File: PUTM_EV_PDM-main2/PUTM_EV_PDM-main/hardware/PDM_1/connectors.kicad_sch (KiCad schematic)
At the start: 3 parts, among them J3 UPT-08-03.0-01-L-V, J4 UPT-08-03.0-01-L-V, J5 UPT-02-01-01-X-RA

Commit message: piny na płytce
Dodano ułożenie pinów na płytce
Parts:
- removed J3, J4: UPT-08-03.0-01-L-V, UPT-08-03.0-01-L-V:SAMTEC_UPT-08-03.0-01-L-V, symbol 8pin:UPT-08-03.0-01-L-V
- added J2, J7: UPT-08-01-01-L-RA, UPT080101LRA, symbol 8pin_good:UPT-08-01-01-L-RA
- added J6: Conn_01x06, Connector_IDC:IDC-Header_2x03_P2.54mm_Vertical, symbol Connector_Generic:Conn_01x06
- J5: footprint UPT-02-01-01-X-RA:SAMTEC_UPT-02-01-01-X-RA -> 2pin:SAMTEC_UPT-02-01-01-X-RA
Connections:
- net +BATT: now reaches J5.P01_1 (01)
- net GND: now reaches J5.P02_1 (02)
- net GND: now also J6.4 (Pin_4), J6.5 (Pin_5), J6.6 (Pin_6), J7.A1, J7.A2, J7.A3, J7.A4, J7.A5, J7.A6
- new net ASMS: J6.3 (Pin_3)
- new net CAN_H: J6.2 (Pin_2)
- new net CAN_L: J6.1 (Pin_1)
- new net OUT1_0: J2.A1, J2.A2, J2.A3, J2.A4, J2.A5, J2.A6
- new net OUT1_1: J2.B1, J2.B2, J2.B3, J2.B4, J2.B5, J2.B6
- new net OUT1_2: J2.C1, J2.C2, J2.C3, J2.C4, J2.C5, J2.C6
- new net OUT1_3: J2.D1, J2.D2, J2.D3, J2.D4, J2.D5, J2.D6
- new net OUT2_0: J2.E1, J2.E2, J2.E3, J2.E4, J2.E5, J2.E6
- new net OUT2_1: J2.F1, J2.F2, J2.F3, J2.F4, J2.F5, J2.F6
- new net OUT2_2: J2.G1, J2.G2, J2.G3, J2.G4, J2.G5, J2.G6
- new net OUT2_3: J2.H1, J2.H2, J2.H3, J2.H4, J2.H5, J2.H6
- new net OUT3_0: J7.B1, J7.B2, J7.B3, J7.B4, J7.B5, J7.B6
- new net OUT3_1: J7.C1, J7.C2, J7.C3, J7.C4, J7.C5, J7.C6
- new net OUT3_2: J7.D1, J7.D2, J7.D3, J7.D4, J7.D5, J7.D6
- new net OUT3_3: J7.E1, J7.E2, J7.E3, J7.E4, J7.E5, J7.E6
- new net OUT4_0: J7.F1, J7.F2, J7.F3, J7.F4, J7.F5, J7.F6
- new net OUT4_1: J7.G1, J7.G2, J7.G3, J7.G4, J7.G5, J7.G6
- new net OUT4_2: J7.H1, J7.H2, J7.H3, J7.H4, J7.H5, J7.H6
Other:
- note added: "trzeba ogarnac"
- moved on the sheet: J5

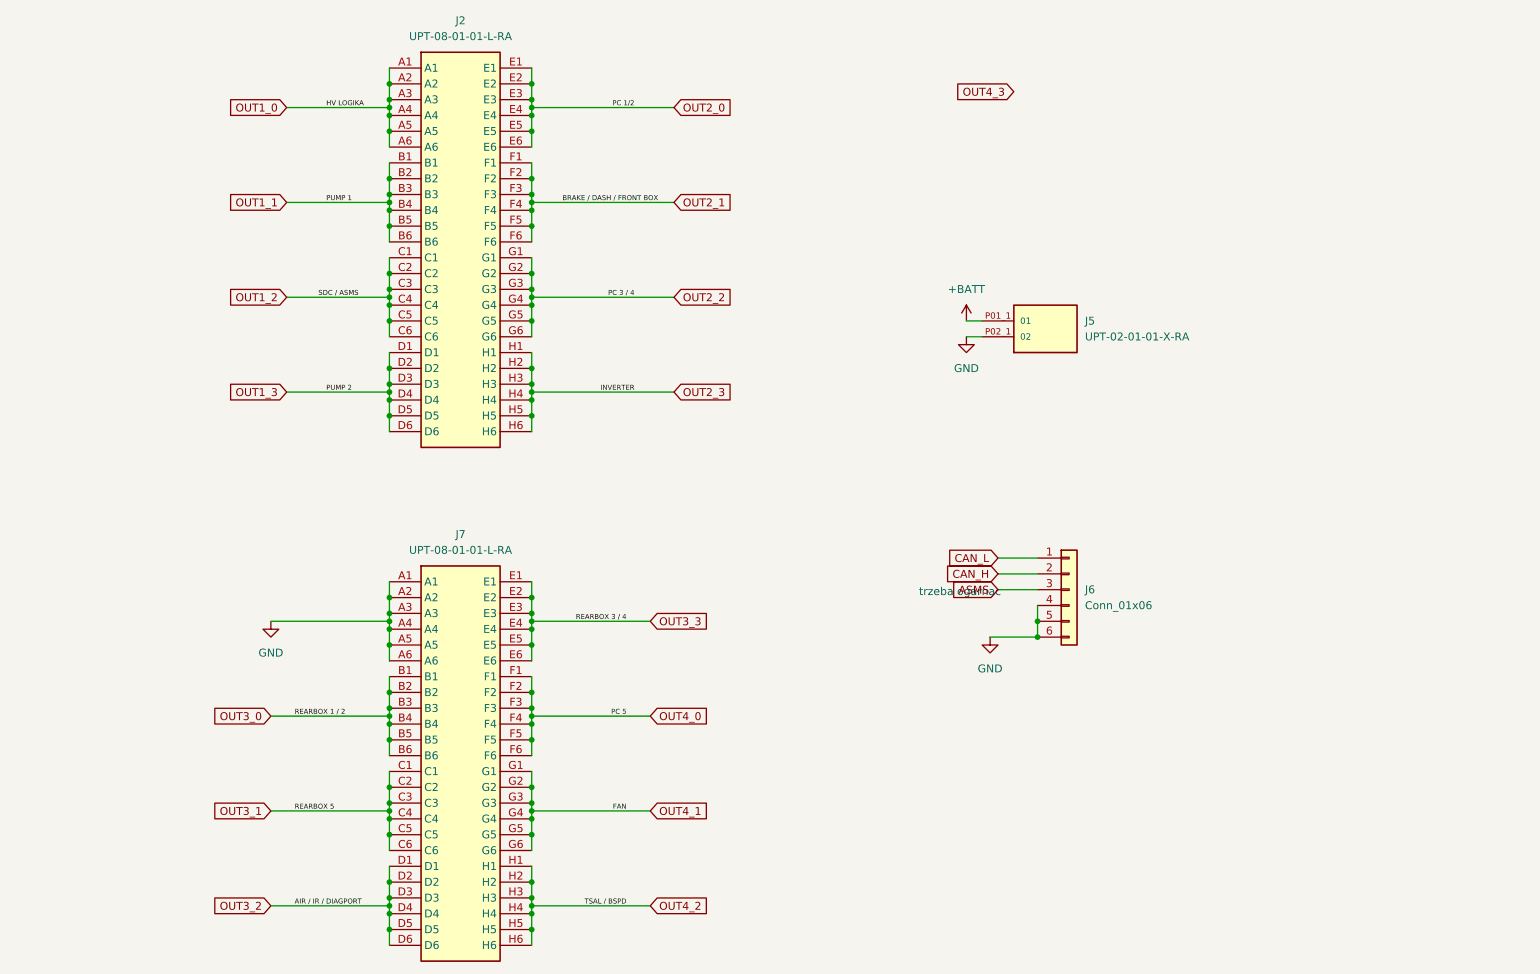
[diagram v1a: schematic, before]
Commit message: Koniec połączeń sygnałów
Wszystkie sygnały z stm poprowadzone
Zmienione ułożenie połączeń do złącz
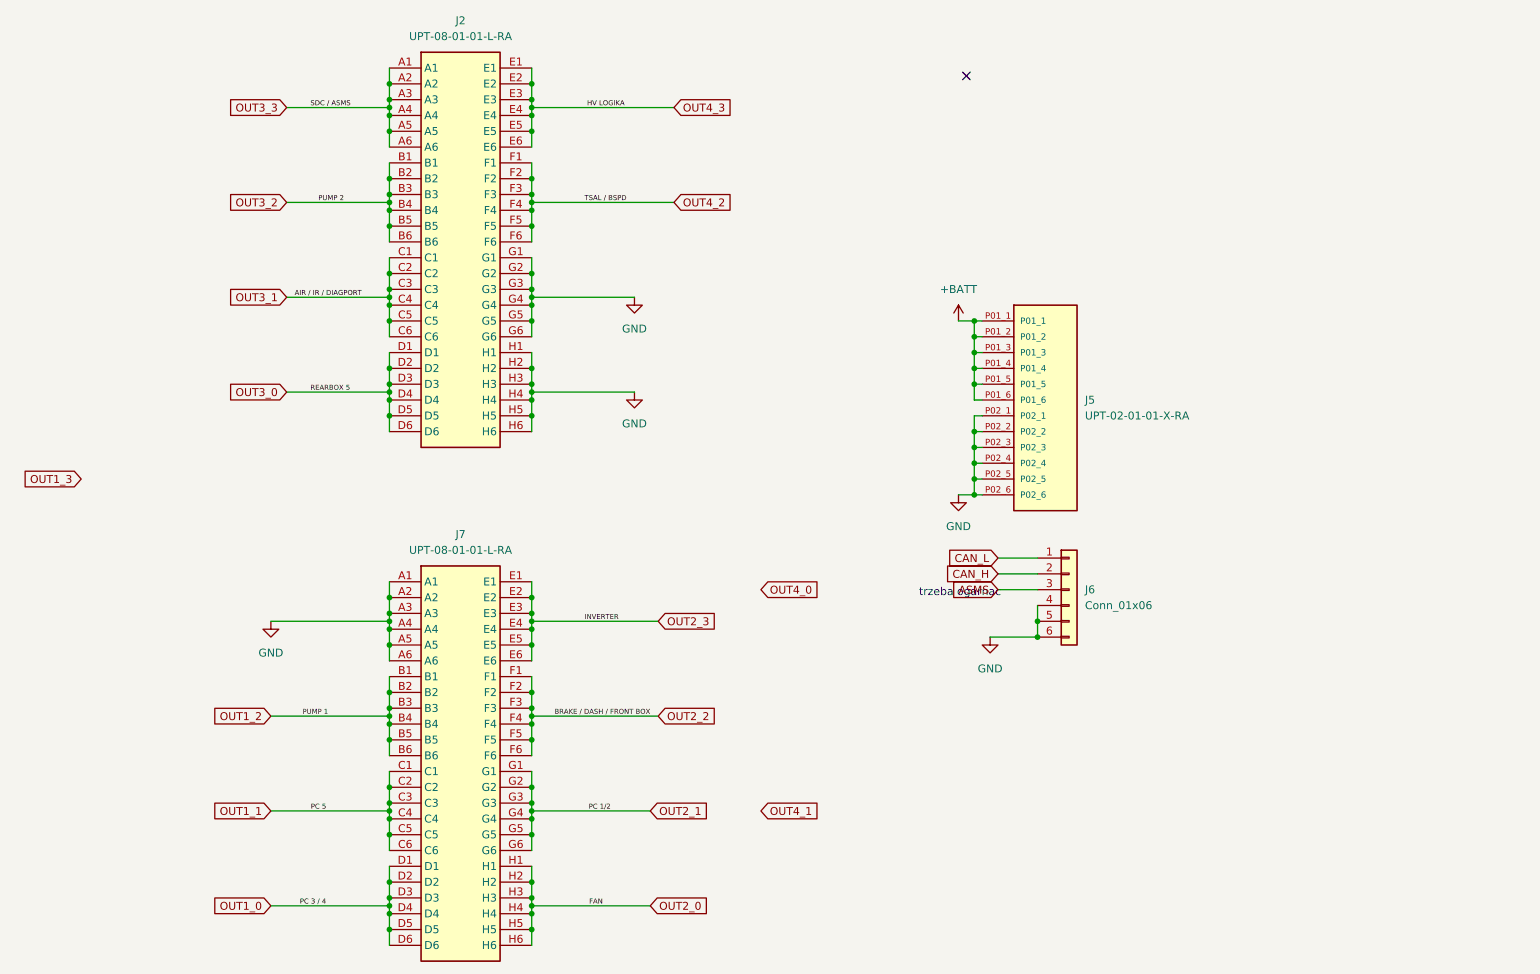
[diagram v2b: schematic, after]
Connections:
- net +BATT: now also J5.P01_2, J5.P01_3, J5.P01_4, J5.P01_5, J5.P01_6
- net GND: now also J2.G1, J2.G2, J2.G3, J2.G4, J2.G5, J2.G6, J2.H1, J2.H2, J2.H3, J2.H4, J2.H5, J2.H6, J5.P02_2, J5.P02_3, J5.P02_4, J5.P02_5, J5.P02_6
- net OUT1_0: now also J7.D1, J7.D2, J7.D3, J7.D4, J7.D5, J7.D6; no longer J2.A1, J2.A2, J2.A3, J2.A4, J2.A5, J2.A6
- net OUT1_1: now also J7.C1, J7.C2, J7.C3, J7.C4, J7.C5, J7.C6; no longer J2.B1, J2.B2, J2.B3, J2.B4, J2.B5, J2.B6
- net OUT1_2: now also J7.B1, J7.B2, J7.B3, J7.B4, J7.B5, J7.B6; no longer J2.C1, J2.C2, J2.C3, J2.C4, J2.C5, J2.C6
- net OUT1_3: no longer J2.D1, J2.D2, J2.D3, J2.D4, J2.D5, J2.D6
- net OUT2_0: now also J7.H1, J7.H2, J7.H3, J7.H4, J7.H5, J7.H6; no longer J2.E1, J2.E2, J2.E3, J2.E4, J2.E5, J2.E6
- net OUT2_1: now also J7.G1, J7.G2, J7.G3, J7.G4, J7.G5, J7.G6; no longer J2.F1, J2.F2, J2.F3, J2.F4, J2.F5, J2.F6
- net OUT2_2: now also J7.F1, J7.F2, J7.F3, J7.F4, J7.F5, J7.F6; no longer J2.G1, J2.G2, J2.G3, J2.G4, J2.G5, J2.G6
- net OUT2_3: now also J7.E1, J7.E2, J7.E3, J7.E4, J7.E5, J7.E6; no longer J2.H1, J2.H2, J2.H3, J2.H4, J2.H5, J2.H6
- net OUT3_0: now also J2.D1, J2.D2, J2.D3, J2.D4, J2.D5, J2.D6; no longer J7.B1, J7.B2, J7.B3, J7.B4, J7.B5, J7.B6
- net OUT3_1: now also J2.C1, J2.C2, J2.C3, J2.C4, J2.C5, J2.C6; no longer J7.C1, J7.C2, J7.C3, J7.C4, J7.C5, J7.C6
- net OUT3_2: now also J2.B1, J2.B2, J2.B3, J2.B4, J2.B5, J2.B6; no longer J7.D1, J7.D2, J7.D3, J7.D4, J7.D5, J7.D6
- net OUT3_3: now also J2.A1, J2.A2, J2.A3, J2.A4, J2.A5, J2.A6; no longer J7.E1, J7.E2, J7.E3, J7.E4, J7.E5, J7.E6
- net OUT4_0: no longer J7.F1, J7.F2, J7.F3, J7.F4, J7.F5, J7.F6
- net OUT4_1: no longer J7.G1, J7.G2, J7.G3, J7.G4, J7.G5, J7.G6
- net OUT4_2: now also J2.F1, J2.F2, J2.F3, J2.F4, J2.F5, J2.F6; no longer J7.H1, J7.H2, J7.H3, J7.H4, J7.H5, J7.H6
- net OUT4_3: now also J2.E1, J2.E2, J2.E3, J2.E4, J2.E5, J2.E6
- no-connect marks 0 -> 1

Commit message: Nowe połączenia
dodana warstwa gnd
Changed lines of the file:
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@@
     )
   )
-  (global_label "OUT4_1" (shape input) (at 143.51 152.4 0) (fields_autoplaced)
+  (global_label "OUT4_1" (shape input) (at 25.4 149.86 0) (fields_autoplaced)
     (effects (font (size 1.27 1.27)) (justify left))
-    (property "Intersheetrefs" "${INTERSHEET_REFS}" (at 153.5104 152.4 0)
+    (property "Intersheetrefs" "${INTERSHEET_REFS}" (at 35.4004 149.86 0)
       (effects (font (size 1.27 1.27)) (justify left) hide)
     )
@@
     )
   )
-  (global_label "OUT4_0" (shape input) (at 143.51 116.84 0) (fields_autoplaced)
+  (global_label "OUT4_0" (shape input) (at 25.4 114.3 0) (fields_autoplaced)
     (effects (font (size 1.27 1.27)) (justify left))
-    (property "Intersheetrefs" "${INTERSHEET_REFS}" (at 153.5104 116.84 0)
+    (property "Intersheetrefs" "${INTERSHEET_REFS}" (at 35.4004 114.3 0)
       (effects (font (size 1.27 1.27)) (justify left) hide)
     )
